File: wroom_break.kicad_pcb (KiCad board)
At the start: 2 copper layers, 21.6 x 21 mm, 3 parts, among them J1 HEADER_8, J2 HEADER_8, U1 ESP-13-WROOM-02

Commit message: Add opensource hardware logo
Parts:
- added G***: LOGO, oshw-logo:oshw-3p4mm, B.Cu at (151.9, 114.9)

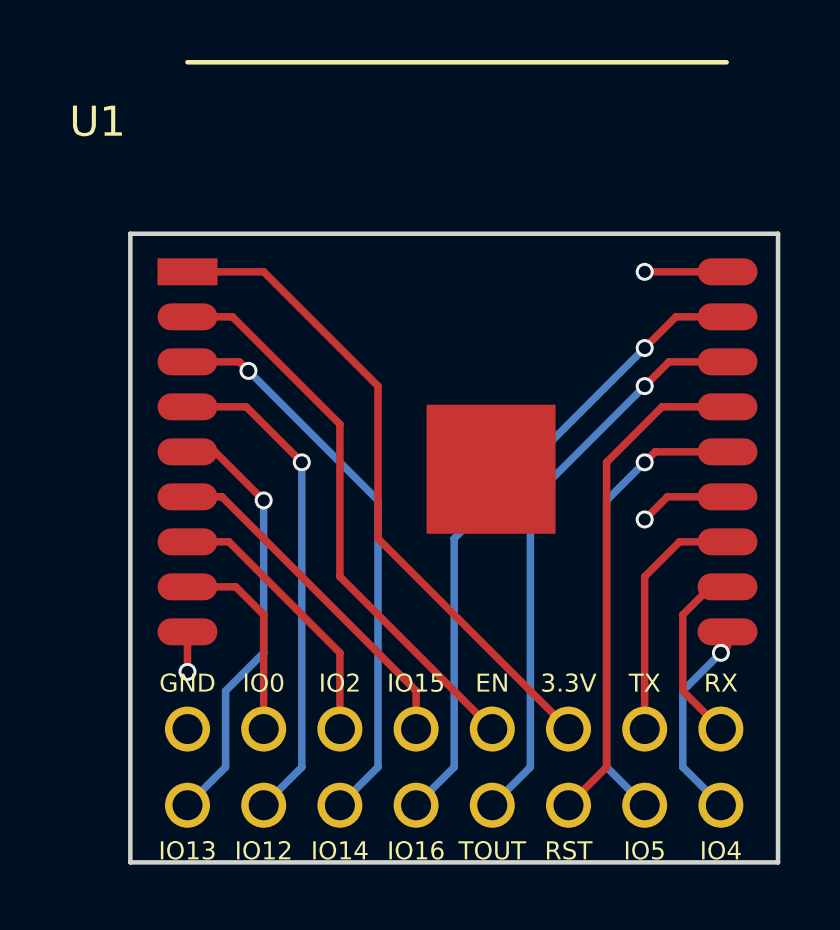
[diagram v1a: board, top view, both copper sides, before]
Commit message: Change board name and vias position
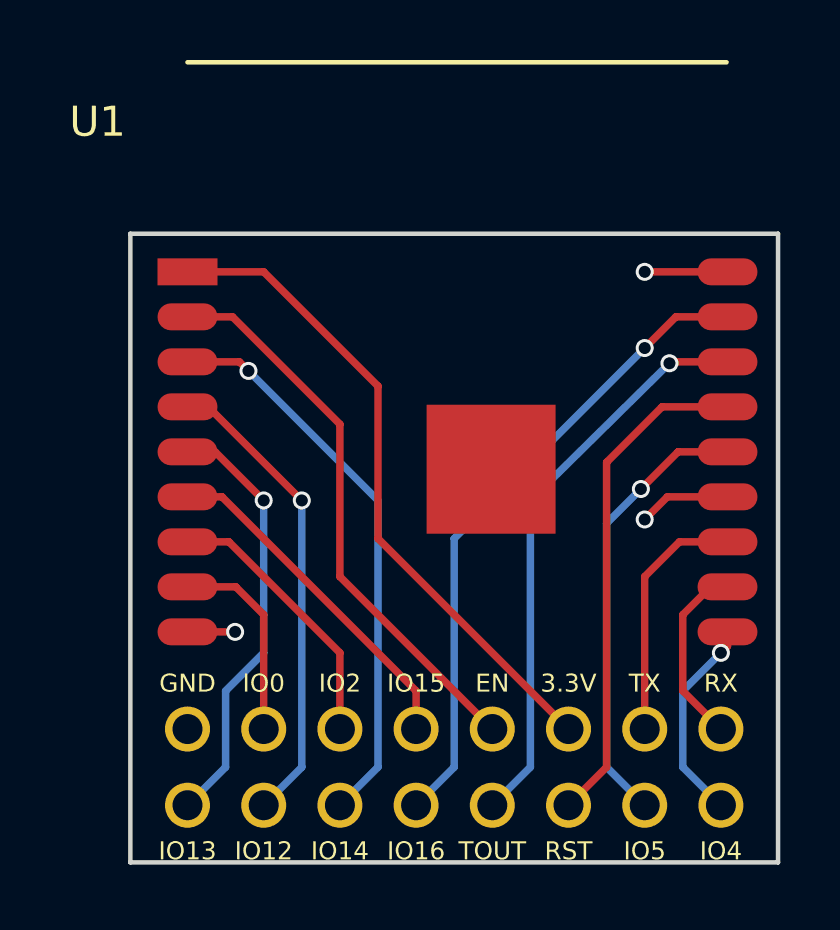
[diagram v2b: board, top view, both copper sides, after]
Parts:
- moved G*** 0.63 mm to (151.5, 115.4)
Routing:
- net Net-(J2-Pad7): track 16.5 -> 15.8 mm
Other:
- board text added: "Rev 1.1"
- board text added: "github.com/asukiaaa/ esp-wroom-02-break"
- board text removed: "asukiaaa/wroom_break"
- board text removed: "ver 1.0"
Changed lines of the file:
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@@
   (layers
     (0 F.Cu signal)
-    (31 B.Cu signal hide)
+    (31 B.Cu signal)
     (32 B.Adhes user)
     (33 F.Adhes user)
@@
   )
   (module oshw-logo:oshw-3p4mm (layer B.Cu)
-    (at 151.892 114.8715 180)
+    (at 151.511 115.3795 180)
     (fp_text reference G*** (at 0 0 180) (layer B.SilkS) hide
       (effects (font (thickness 0.3)) (justify mirror))
@@
       (xy -0.264581 1.278283) (xy -0.227912 1.479826) (xy 0.238956 1.479826) (xy 0.275625 1.278283)) (layer B.SilkS) (width 0.01))
   )
-  (gr_text "ver 1.0\n" (at 157.48 113.538) (layer B.SilkS)
+  (gr_text "Rev 1.1" (at 157.5435 115.062) (layer B.SilkS)
     (effects (font (size 0.8 0.8) (thickness 0.2)) (justify mirror))
   )
-  (gr_text asukiaaa/wroom_break (at 157.48 110.49) (layer B.SilkS)
+  (gr_text "github.com/asukiaaa/\nesp-wroom-02-break" (at 157.48 110.617) (layer B.SilkS)
     (effects (font (size 1.1 1.1) (thickness 0.25)) (justify mirror))
   )
@@
   (via (at 166.37 118.11) (size 0.6) (drill 0.4) (layers F.Cu B.Cu) (net 7))
   (segment (start 166.59 117.89) (end 166.37 118.11) (width 0.25) (layer F.Cu) (net 7))
-  (segment (start 162.56 113.03) (end 162.56 121.92) (width 0.25) (layer B.Cu) (net 8))
-  (segment (start 166.59 111.41) (end 164.18 111.41) (width 0.25) (layer F.Cu) (net 8))
-  (segment (start 162.56 121.92) (end 163.83 123.19) (width 0.25) (layer B.Cu) (net 8))
-  (segment (start 163.83 111.76) (end 162.56 113.03) (width 0.25) (layer B.Cu) (net 8))
-  (via (at 163.83 111.76) (size 0.6) (drill 0.4) (layers F.Cu B.Cu) (net 8))
-  (segment (start 164.18 111.41) (end 163.83 111.76) (width 0.25) (layer F.Cu) (net 8))
+  (segment (start 162.56 113.792) (end 163.703 112.649) (width 0.25) (layer B.Cu) (net 8))
+  (segment (start 162.56 113.792) (end 162.56 121.92) (width 0.25) (layer B.Cu) (net 8))
+  (segment (start 163.83 123.19) (end 162.56 121.92) (width 0.25) (layer B.Cu) (net 8))
+  (segment (start 164.942 111.41) (end 166.59 111.41) (width 0.25) (layer F.Cu) (net 8) (status 800000))
+  (segment (start 163.703 112.649) (end 164.942 111.41) (width 0.25) (layer F.Cu) (net 8))
+  (via (at 163.703 112.649) (size 0.6) (drill 0.4) (layers F.Cu B.Cu) (net 8))
   (segment (start 166.59 109.91) (end 164.41 109.91) (width 0.25) (layer F.Cu) (net 9))
   (segment (start 162.56 121.92) (end 161.29 123.19) (width 0.25) (layer F.Cu) (net 9))
@@
   (segment (start 166.59 108.41) (end 164.64 108.41) (width 0.25) (layer F.Cu) (net 10))
   (segment (start 160.02 121.92) (end 158.75 123.19) (width 0.25) (layer B.Cu) (net 10))
-  (segment (start 163.83 109.22) (end 160.02 113.03) (width 0.25) (layer B.Cu) (net 10))
-  (via (at 163.83 109.22) (size 0.6) (drill 0.4) (layers F.Cu B.Cu) (net 10))
-  (segment (start 164.64 108.41) (end 163.83 109.22) (width 0.25) (layer F.Cu) (net 10))
+  (segment (start 164.6555 108.458) (end 160.02 113.03) (width 0.25) (layer B.Cu) (net 10))
+  (via (at 164.6555 108.458) (size 0.6) (drill 0.4) (layers F.Cu B.Cu) (net 10))
+  (segment (start 164.64 108.41) (end 164.6555 108.458) (width 0.25) (layer F.Cu) (net 10))
   (segment (start 157.48 114.3) (end 157.48 121.92) (width 0.25) (layer B.Cu) (net 11))
   (segment (start 166.59 106.91) (end 164.87 106.91) (width 0.25) (layer F.Cu) (net 11))
@@
   (segment (start 151.13 116.84) (end 151.13 120.65) (width 0.25) (layer F.Cu) (net 13))
   (segment (start 150.2 115.91) (end 151.13 116.84) (width 0.25) (layer F.Cu) (net 13))
-  (segment (start 148.59 117.41) (end 148.59 118.745) (width 0.25) (layer F.Cu) (net 14))
-  (via (at 148.59 118.745) (size 0.6) (drill 0.4) (layers F.Cu B.Cu) (net 14))
+  (segment (start 148.59 117.41) (end 150.1775 117.4115) (width 0.25) (layer F.Cu) (net 14))
+  (via (at 150.1775 117.4115) (size 0.6) (drill 0.4) (layers F.Cu B.Cu) (net 14))
   (segment (start 166.59 105.41) (end 163.83 105.41) (width 0.25) (layer F.Cu) (net 14))
   (via (at 163.83 105.41) (size 0.6) (drill 0.4) (layers F.Cu B.Cu) (net 14))
@@
   (via (at 163.83 113.665) (size 0.6) (drill 0.4) (layers F.Cu B.Cu) (net 14))
   (segment (start 164.585 112.91) (end 163.83 113.665) (width 0.25) (layer F.Cu) (net 14))
-  (segment (start 148.59 109.91) (end 150.55 109.91) (width 0.25) (layer F.Cu) (net 15))
+  (segment (start 148.59 109.91) (end 149.28 109.91) (width 0.25) (layer F.Cu) (net 15))
+  (segment (start 149.28 109.91) (end 152.4 113.03) (width 0.25) (layer F.Cu) (net 15))
   (segment (start 152.4 121.92) (end 151.13 123.19) (width 0.25) (layer B.Cu) (net 15))
-  (segment (start 152.4 111.76) (end 152.4 121.92) (width 0.25) (layer B.Cu) (net 15))
-  (via (at 152.4 111.76) (size 0.6) (drill 0.4) (layers F.Cu B.Cu) (net 15))
-  (segment (start 150.55 109.91) (end 152.4 111.76) (width 0.25) (layer F.Cu) (net 15))
+  (segment (start 152.4 113.03) (end 152.4 121.92) (width 0.25) (layer B.Cu) (net 15))
+  (via (at 152.4 113.03) (size 0.6) (drill 0.4) (layers F.Cu B.Cu) (net 15))
   (segment (start 151.13 118.11) (end 149.86 119.38) (width 0.25) (layer B.Cu) (net 16))
   (segment (start 149.86 119.38) (end 149.86 121.92) (width 0.25) (layer B.Cu) (net 16))
